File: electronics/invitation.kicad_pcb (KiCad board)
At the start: 2 copper layers, 57 x 86 mm, 16 parts, among them P1 USB_OTG, U1 ATMEGA32U4-A, X1 16 MHz

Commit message: Commit 37: Electronics business card initial design
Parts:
- removed X1: 16 MHz, Crystals:Resonator_7.2x3mm
- added C3: 22pF, Capacitors_SMD:C_0805, B.Cu at (185.2, 78.5)
- added C5: 22pF, Capacitors_SMD:C_0805, B.Cu at (181.1, 78.5)
- added D1: Power LED, LEDs:LED_0402, B.Cu at (185.2, 98.8)
- added D4: TX LED, LEDs:LED_0402, B.Cu at (170.7, 73.2)
- added D5: RX LED, LEDs:LED_0402, B.Cu at (170.7, 74.7)
- added G***: LOGO, assets:mail, B.Cu at (186.2, 124.5)
- added G***: LOGO, assets:phone, B.Cu at (154.2, 124.0)
- added P10: Tassimo, assets:tassimoButton, F.Cu at (186.9, 99.8)
- added P11: Maker, assets:makerButton, F.Cu at (162.1, 113.3)
- added P2: James Miller, assets:JMLogoButton, F.Cu at (162.1, 99.8)
- added P3: CONN_02X03, assets:Programming_port, B.Cu at (127.0, 73.7)
- added P4: D&AD, assets:moodButton, F.Cu at (128.3, 80.3)
- added P5: Krispy Kreme, assets:krispyButton, F.Cu at (196.1, 80.3)
- added P6: Epic Mind Drive, assets:mindDriveButton, F.Cu at (128.3, 119.1)
- added P7: Hacky Xmas, assets:hackyButton, F.Cu at (196.1, 119.1)
- added P8: Pay@Pump, assets:beerButton, F.Cu at (162.1, 86.4)
- added P9: WIYWI, assets:WiywiButton, F.Cu at (137.4, 99.8)
- added R4: 330, Resistors_SMD:R_0402, B.Cu at (147.3, 73.7)
- added R7: 330, Resistors_SMD:R_0402, B.Cu at (151.9, 76.2)
- added R8: 330, Resistors_SMD:R_0402, B.Cu at (147.3, 76.2)
- added Y1: Crystal_Small, Crystals:Crystal_HC49-SD_SMD, B.Cu at (181.1, 74.7)
- C1, C2, C4, C6, C7, F1, P1, R1, R2, R3, R5, R6, U1: moved to B.Cu
- D2: value RX LED -> Interaction LED; moved to B.Cu
- D3: value TX LED -> Node LED; moved to B.Cu
- moved R3 102.8 mm to (151.9, 73.7)
- moved C7 99.4 mm to (130.8, 74.7)
- moved C2 97.0 mm to (142.2, 74.7)
- moved C1 96.9 mm to (138.4, 74.7)
- moved C6 94.1 mm to (134.6, 74.7)
- moved R6 93.0 mm to (176.3, 78.5), turned to 0 degrees
- moved P1 91.8 mm to (162.1, 75.4)
- moved F1 90.1 mm to (155.2, 74.9), turned to 90 degrees
- moved R5 88.9 mm to (176.3, 80.0)
- moved D3 75.4 mm to (185.2, 106.7), turned to 90 degrees
- moved D2 75.3 mm to (185.2, 102.9), turned to 90 degrees
- moved R1 69.2 mm to (185.7, 81.8), turned to 180 degrees
- moved R2 66.9 mm to (185.7, 83.3), turned to 180 degrees
- moved C4 62.3 mm to (189.0, 83.6), turned to 180 degrees
- moved U1 58.3 mm to (197.1, 79.0), turned to 0 degrees
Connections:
- net Net-(R3-Pad1) renamed RESET
- D2 pad 2: VCC -> interactLED
- D3 pad 2: VCC -> nodeLED
- R5 pad 2: Net-(D2-Pad1) -> Net-(D5-Pad1)
- R6 pad 1: Net-(D3-Pad1) -> Net-(D4-Pad1)
- U1 pad 1: Net-(U1-Pad1) -> portfolio5Btn
- U1 pad 10: Net-(U1-Pad10) -> MOSI
- U1 pad 11: Net-(U1-Pad11) -> MISO
- U1 pad 18: Net-(U1-Pad18) -> portfolio2Btn
- U1 pad 19: Net-(U1-Pad19) -> portfolio1Btn
- U1 pad 25: Net-(U1-Pad25) -> portfolio3Btn
- U1 pad 27: Net-(U1-Pad27) -> portfolio4Btn
- U1 pad 28: Net-(U1-Pad28) -> portfolio6Btn
- U1 pad 29: Net-(U1-Pad29) -> nodeLED
- U1 pad 30: Net-(U1-Pad30) -> interactLED
- U1 pad 9: Net-(U1-Pad9) -> SCLK
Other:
- board size 57 x 86 mm -> 86 x 57 mm
- board text added: "+44 (0)7960644904"
- board text added: "Connect this card to your computer using the cable Open in a web browser Tap the buttons below to explore"
- board text added: "How to access James' portfolio:"
- board text added: "info@jamesmillerportfolio.co.uk"
- board text added: "www.jamesmillerportfolio.co.uk"
- board text removed: "1: Plug the usb into your computer. 2: Open "http://www.jamesmillerportfolio.co.uk" in a web browser. 3: Tap the buttons below to explore the website."
- board text removed: "Instructions"

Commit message: Commit 38: Business card pre-production
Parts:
- removed the P2 at (162.1, 99.8)
- added G***: LOGO, assets:beerSS, F.Cu at (162.1, 86.4)
- added G***: LOGO, assets:WIYWISS, F.Cu at (137.4, 99.8)
- added G***: LOGO, assets:JMLogoSS, F.Cu at (161.8, 99.8)
- added G***: LOGO, assets:WIYWI-F.Mask, F.Cu at (137.4, 99.8)
- added G***: LOGO, assets:makerGif-F.Mask, F.Cu at (162.1, 113.3)
- added G***: LOGO, assets:krispyKreme-F.Mask, F.Cu at (196.3, 80.3)
- added G***: LOGO, assets:tassimoGif-F.Mask, F.Cu at (186.9, 99.3)
- added G***: LOGO, assets:hackyXmas-F.Mask, F.Cu at (196.1, 119.1)
- added G***: LOGO, assets:WIYWI-F.Cu, F.Cu at (137.4, 99.8)
- added G***: LOGO, assets:makerGif-F.Cu, F.Cu at (162.1, 113.3)
- added G***: LOGO, assets:hackyXmas-F.Cu, F.Cu at (196.1, 119.1)
- added G***: LOGO, assets:tassimoGif-F.Cu, F.Cu at (186.9, 99.3)
- added G***: LOGO, assets:krispyKreme-F.Cu, F.Cu at (196.3, 80.3)
- added G***: LOGO, assets:moodTreeGif-F.Mask, F.Cu at (128.3, 79.8)
- added G***: LOGO, assets:moodTreeGif-F.Cu, F.Cu at (128.3, 79.8)
- added G***: LOGO, assets:beerGif-F.Mask, F.Cu at (162.1, 86.4)
- added G***: LOGO, assets:beerGif, F.Cu at (162.1, 86.4)
- added G***: LOGO, assets:mindDrive-F.Mask, F.Cu at (128.5, 118.9)
- added G***: LOGO, assets:mindDrive, F.Cu at (128.5, 118.9)
- added G***: LOGO, assets:moodTreeGifSS, F.Cu at (128.3, 79.8)
- added G***: LOGO, assets:mindDriveSS, F.Cu at (128.5, 118.9)
- added G***: LOGO, assets:makerGifSS, F.Cu at (162.1, 113.3)
- added G***: LOGO, assets:hackyXmasSS, F.Cu at (196.1, 119.1)
- added G***: LOGO, assets:tassimoSS, F.Cu at (186.9, 99.3)
- added G***: LOGO, assets:krispyKremeSS, F.Cu at (196.3, 80.3)
- added P2: James Miller, assets:JMLogo, F.Cu at (161.8, 99.8)
- added P2: James Miller, assets:JMLogo-F.Mask, F.Cu at (161.8, 99.8)
- added P2: James Miller, assets:JMLogo-F.Cu, F.Cu at (161.8, 99.8)
- C3, C5: footprint Capacitors_SMD:C_0805 -> Capacitors_SMD:C_0402
- P10: footprint assets:tassimoButton -> assets:tassimoGif
- P11: footprint assets:makerButton -> assets:makerGif
- P4: footprint assets:moodButton -> assets:moodTreeGif
- P5: footprint assets:krispyButton -> assets:krispyKreme
- P6: footprint assets:mindDriveButton -> assets:mindDrive-F.Paste
- P7: footprint assets:hackyButton -> assets:hackyXmas
- P8: footprint assets:beerButton -> assets:beerGif-F.Paste
- P9: footprint assets:WiywiButton -> assets:WIYWI
- Y1: footprint Crystals:Crystal_HC49-SD_SMD -> assets:crystal_FA238-TSX3225
- moved R5 39.4 mm to (137.4, 73.7), turned to 180 degrees
- moved D4 39.0 mm to (131.8, 76.2)
- moved R6 38.9 mm to (137.4, 76.2)
- moved D5 38.9 mm to (131.8, 73.7)
- moved C6 38.9 mm to (173.5, 74.7)
- moved C7 38.6 mm to (169.4, 74.7)
- moved C2 35.3 mm to (177.5, 74.7)
- moved C1 16.3 mm to (154.7, 74.7)
- moved C4 13.2 mm to (180.6, 73.4), turned to 90 degrees
- moved C5 9.80 mm to (189.5, 73.4), turned to 270 degrees
- moved C3 5.57 mm to (182.9, 73.4), turned to 90 degrees
- moved Y1 5.18 mm to (186.2, 73.7), turned to 0 degrees
- moved R4 5.08 mm to (142.2, 73.7)
- moved R8 5.08 mm to (142.2, 76.2)
- moved F1 4.83 mm to (150.4, 74.9)
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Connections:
- net Net-(P1-Pad2) renamed /Data-
- net Net-(P1-Pad3) renamed /Data+
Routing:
- net MISO: track 0.00 -> 166.5 mm, vias 0 -> 2
- net RESET: track 0.00 -> 163.2 mm, vias 0 -> 5
- net portfolio3Btn: track 0.00 -> 157.0 mm, vias 0 -> 1
- net MOSI: track 0.00 -> 154.2 mm, vias 0 -> 3
- net GND: track 0.00 -> 153.3 mm, vias 0 -> 15
- net VCC: track 0.00 -> 138.2 mm, vias 0 -> 6
- net SCLK: track 0.00 -> 125.6 mm, vias 0 -> 4
- net portfolio6Btn: track 0.00 -> 119.6 mm, vias 0 -> 1
- net portfolio1Btn: track 0.00 -> 77.7 mm, vias 0 -> 1
- net Net-(R6-Pad2): track 0.00 -> 74.6 mm, vias 0 -> 2
- net Net-(R5-Pad1): track 0.00 -> 59.2 mm, vias 0 -> 2
- net Net-(D2-Pad1): track 0.00 -> 57.0 mm
- net Net-(D1-Pad1): track 0.00 -> 55.5 mm
- net USBVCC: track 0.00 -> 54.6 mm
- net Net-(D3-Pad1): track 0.00 -> 52.7 mm
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- added copper zone on B.Cu, net GND
- added copper zone on F.Cu, net GND
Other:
- net class Data added: clearance 0.1, trace_width 0.12, via_dia 0.6, via_drill 0.4
- net class Default: clearance 0.2 -> 0
- net class Power added: clearance 0, trace_width 0.3, via_dia 0.6, via_drill 0.4
- rule trace_clearance: 0.2 -> 0
- rule trace_min: 0.2 -> 0.1
- board text added: "Connect this card to your PC with the USB cable Open in a web browser Tap the buttons below to explore"
- board text added: "GND"
- board text added: "MISO"
- board text added: "MOSI"
- board text added: "RESET"
- board text added: "SCLK"
- board text added: "VCC"
- board text removed: "Connect this card to your computer using the cable Open in a web browser Tap the buttons below to explore"

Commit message: Commit 39: Business Card V1 Completed
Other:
- board text added: "Connect this card to your PC with the USB cable Open in a web browser Tap the buttons on the reverse side to explore"
- board text removed: "Connect this card to your PC with the USB cable Open in a web browser Tap the buttons below to explore"
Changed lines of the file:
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@@
     (links 88)
     (no_connects 0)
-    (area 119.169999 70.485 206.819715 128.274001)
+    (area 119.169999 71.123999 205.320001 128.274001)
     (thickness 1.6)
     (drawings 21)
@@
       (outputformat 4)
       (mirror false)
-      (drillshape 0)
+      (drillshape 2)
       (scaleselection 1)
       (outputdirectory productionFiles-V1/))
@@
   (gr_line (start 162.56 86.36) (end 161.798 86.36) (angle 90) (layer Dwgs.User) (width 0.2))
   (gr_line (start 162.052 86.106) (end 162.052 86.868) (angle 90) (layer Dwgs.User) (width 0.2))
-  (gr_text "     Connect this card to your PC with the USB cable\n\n     Open                                in a web browser\n\n     Tap the buttons below to explore" (at 187.96 102.87) (layer B.SilkS)
+  (gr_text "     Connect this card to your PC with the USB cable\n\n     Open                                in a web browser\n\n     Tap the buttons on the reverse side to explore" (at 187.96 102.87) (layer B.SilkS)
     (effects (font (size 1.2 1.2) (thickness 0.175)) (justify left mirror))
   )

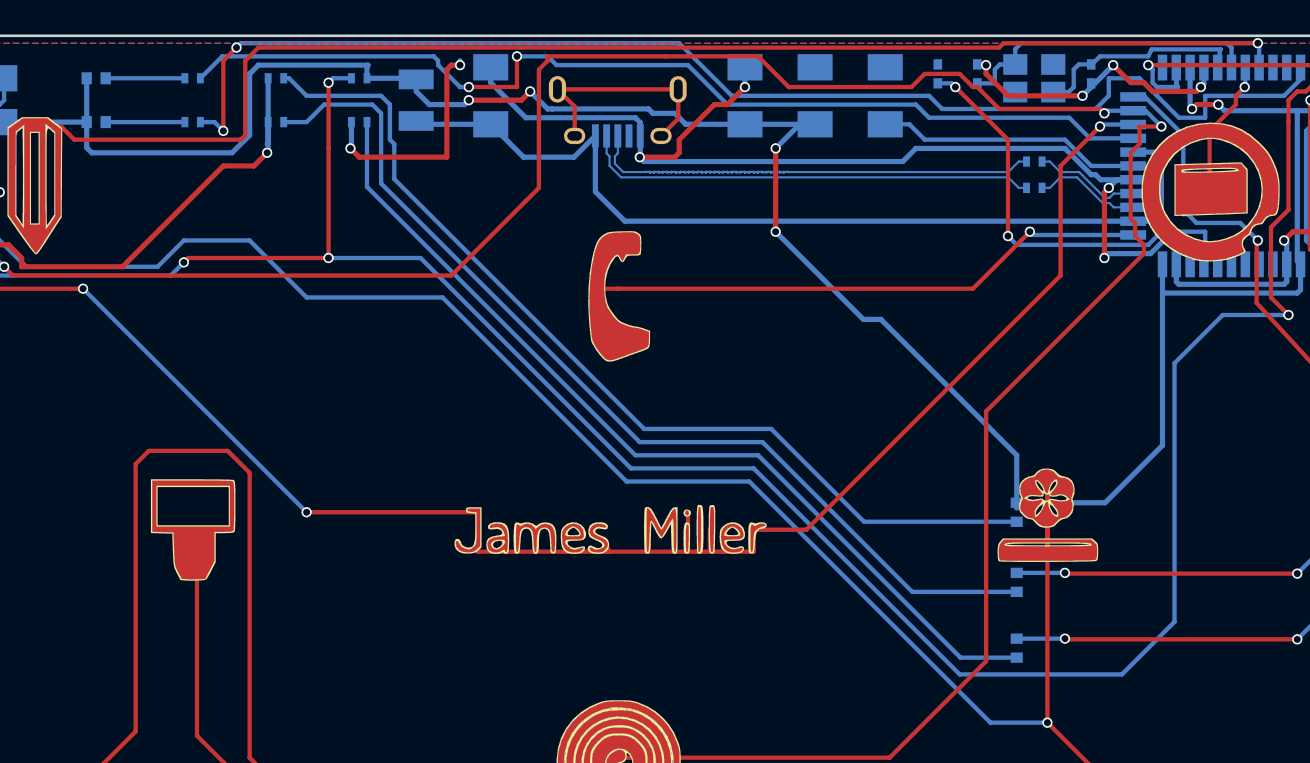
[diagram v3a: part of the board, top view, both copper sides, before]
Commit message: Commit 41: Updated Business Card BOM + PCB + Schematic to make sure components can be sourced.
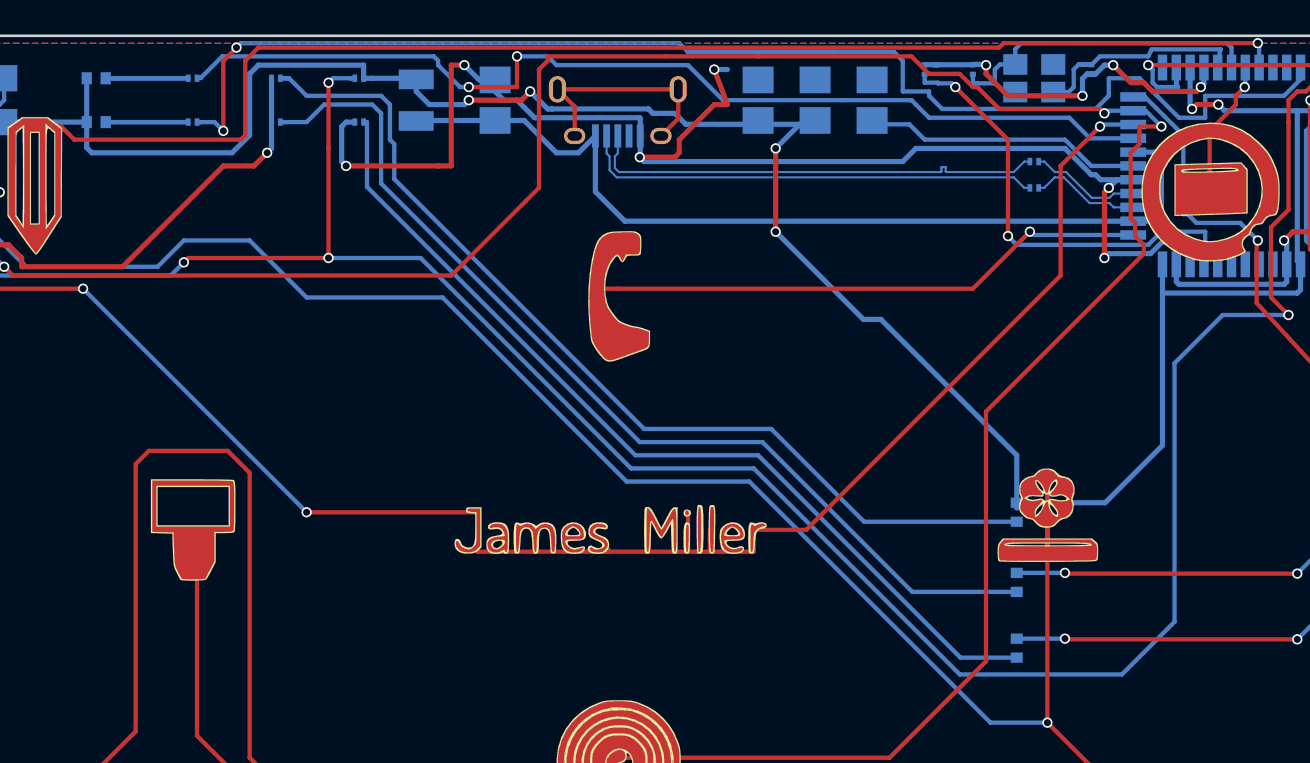
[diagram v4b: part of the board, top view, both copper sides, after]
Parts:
- C1, C2, C6, C7: footprint SMD_Packages:SMD-1206_Pol -> Capacitors_Tantalum_SMD:CP_Tantalum_Case-R_EIA-2012-12_Reflow
- C3, C4, C5: footprint Capacitors_SMD:C_0402 -> Capacitors_SMD:C_0201
- D1: value Power LED -> Power LED (green)
- D2: value Interaction LED -> Interaction LED (green)
- D3: value Node LED -> Node LED (green)
- D4: value TX LED -> TX LED (orange)
- D5: value RX LED -> RX LED (orange)
- F1: value 500mA -> PPTC Fuse 500mA
- P1: value USB_OTG -> USB Micro B
- R1, R2, R3, R4, R5, R6, R7, R8: footprint Resistors_SMD:R_0402 -> Resistors_SMD:R_0201
- Y1: value Crystal_Small -> 16 FA-238 Mhz
- moved C2 0.80 mm to (176.8, 74.9)
- moved C4 0.80 mm to (179.8, 73.2)
- moved C7 0.80 mm to (170.2, 74.9)
- moved C1 0.36 mm to (154.9, 74.9)
- moved C3 0.36 mm to (182.6, 73.2)
- moved C5 0.25 mm to (189.5, 73.2)
- moved C6 0.25 mm to (173.5, 74.9)
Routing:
- net GND: track 153.3 -> 160.4 mm
- net Net-(D5-Pad1): track 4.59 -> 9.37 mm
- net Net-(D4-Pad1): track 4.59 -> 9.37 mm
- net Net-(R6-Pad2): track 74.6 -> 76.1 mm
- net Net-(C4-Pad1): track 25.7 -> 27.0 mm
- net Net-(C3-Pad1): track 17.9 -> 18.7 mm
- net MOSI: track 154.2 -> 153.6 mm
- net Net-(D1-Pad1): track 55.5 -> 56.0 mm

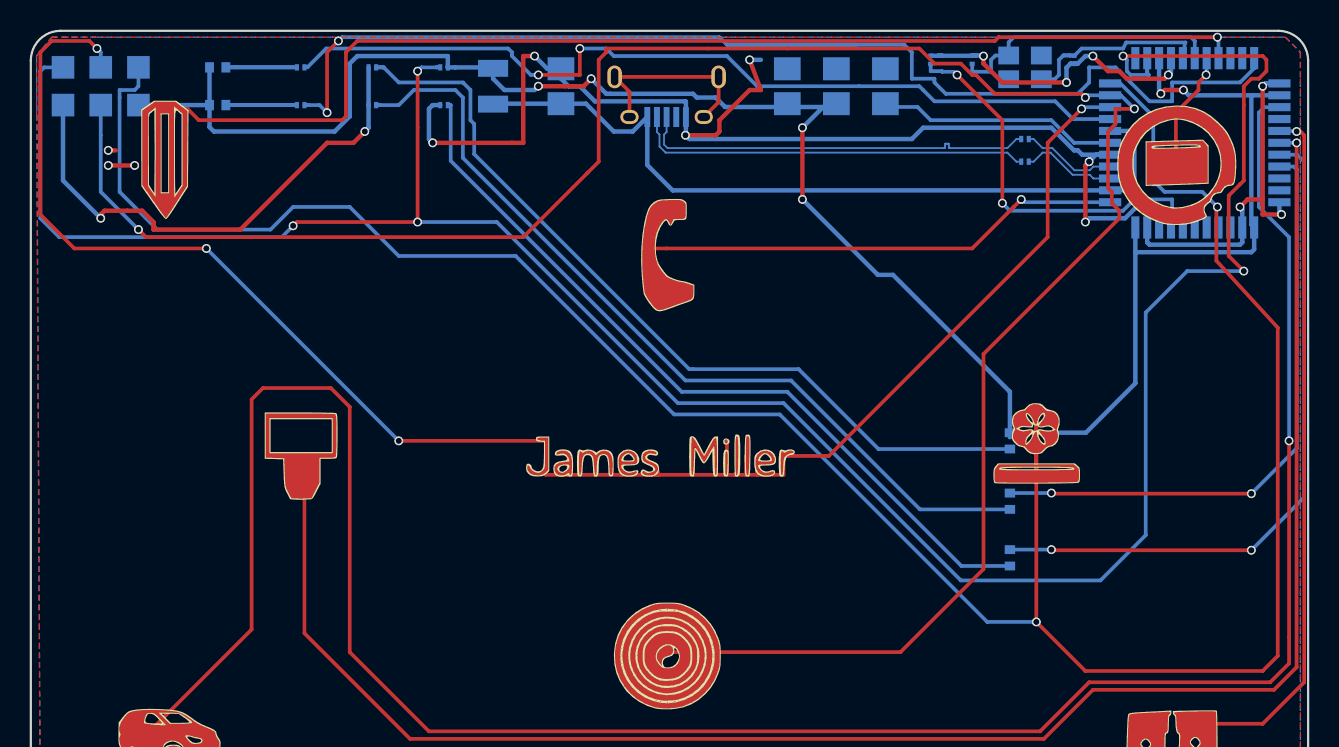
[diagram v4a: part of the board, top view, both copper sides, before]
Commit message: Commit 47: Latest electronic updates, moved via so that there aren't any production issues
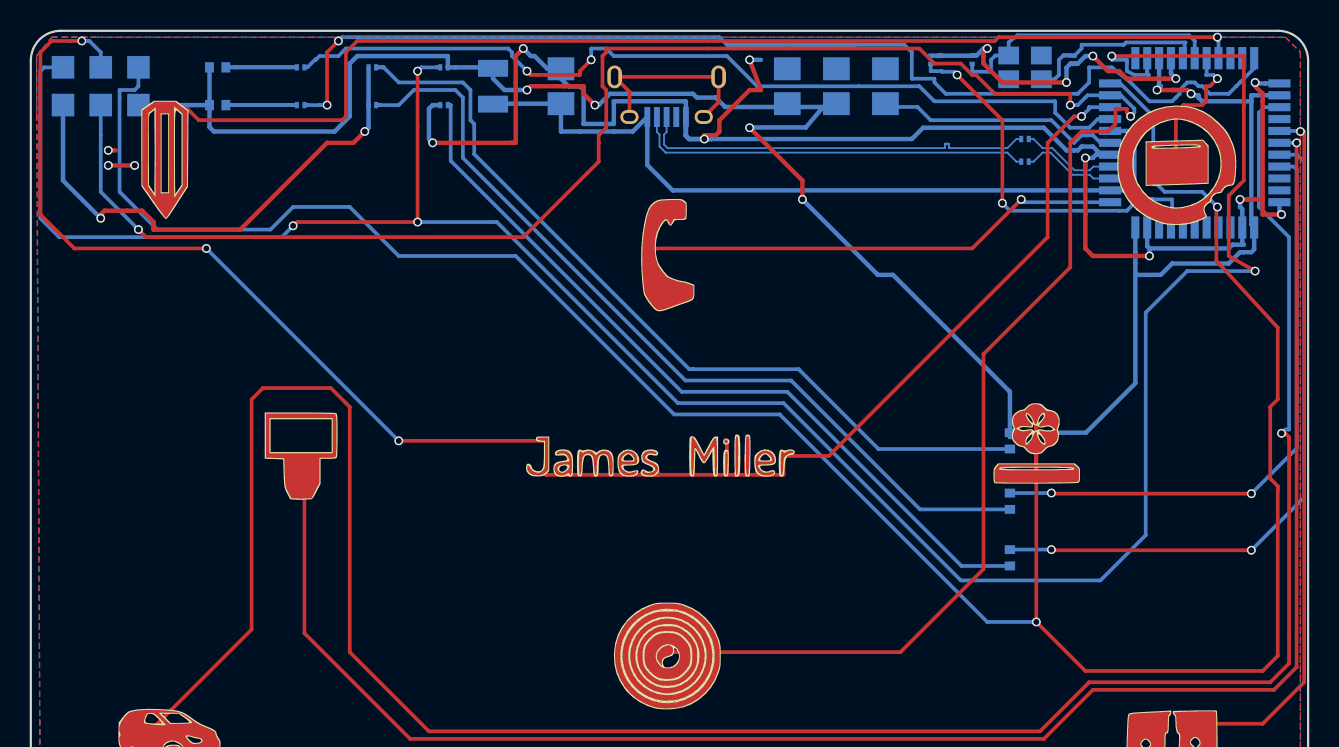
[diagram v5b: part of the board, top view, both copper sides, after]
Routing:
- net GND: track 160.4 -> 171.8 mm
- net VCC: track 138.1 -> 144.9 mm
- net MOSI: track 153.6 -> 155.8 mm
- net portfolio2Btn: track 13.0 -> 14.8 mm
- net USBVCC: track 54.1 -> 55.2 mm
- net Net-(C4-Pad1): track 27.0 -> 28.0 mm
- net RESET: track 163.4 -> 164.4 mm
- net Net-(R6-Pad2): track 76.1 -> 75.3 mm
- net portfolio3Btn: track 157.0 -> 157.7 mm
- net Net-(R5-Pad1): track 59.4 -> 60.0 mm
